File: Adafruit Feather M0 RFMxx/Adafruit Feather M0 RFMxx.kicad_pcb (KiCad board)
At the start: 2 copper layers, 50.8 x 22.9 mm, 39 parts, among them SW1 SPST_TACT-KMR2, U2 AP2112K-3.3, U3 MCP73831T-2ACI/OT, U4 RFM69HCW, X1 JSTPH, X2 32.768, X3 microUSB, X4 uFL

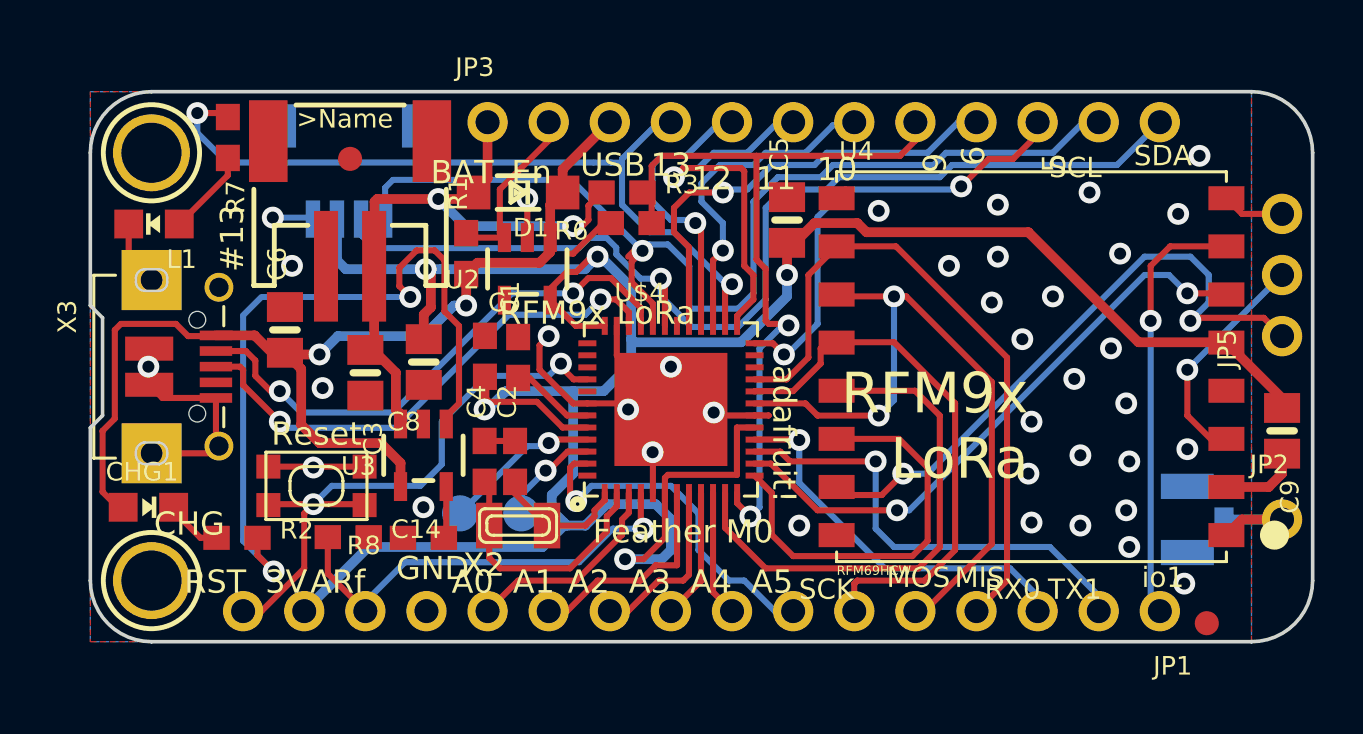
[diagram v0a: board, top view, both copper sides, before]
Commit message: Moving silscreen around and made some invisible. Working on a track near 144, 100.
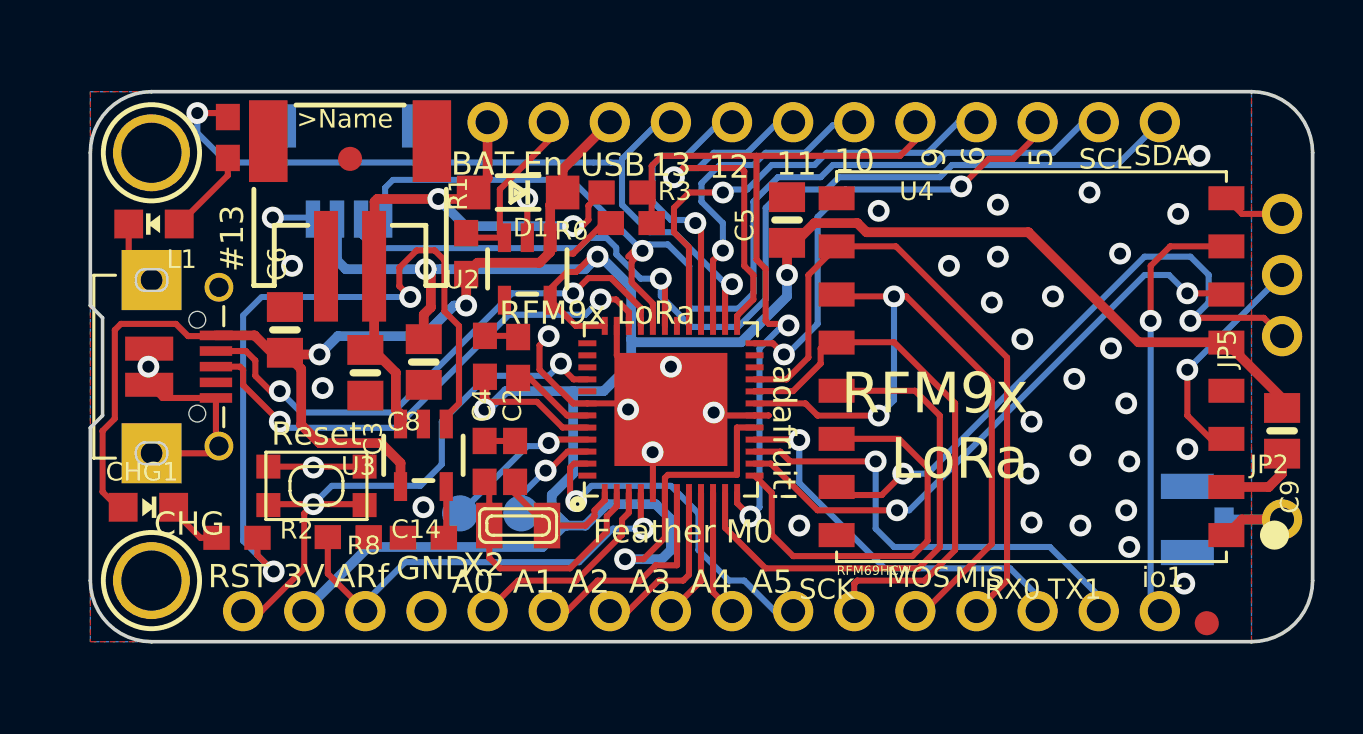
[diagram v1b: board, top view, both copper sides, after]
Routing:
- net GND: track 46.8 -> 47.9 mm

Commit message: Remaining Air wire was caused by ground pour on bottom that had become an island with the addition of the qwiic connector. Rerouted signals in that area to allow it to reconnect with other ground pour.
Now only "not connected" are defined ground area top and bottom.

Added gnd track between voltage sense resistor divider and ground so that it
shows when highlighting the GND net.

Moved track within USB connector to eliminate DRC "track too close to ..." error.

Now only 2 DRC errors are with holes in PCB that are part of X3 (USB connector).

Cleaned up silkscreen.

Plotted gerbers with option to not print silkscreen where there is no soldermask.
Option to not print silkscreen on pads did not seem to do anything.
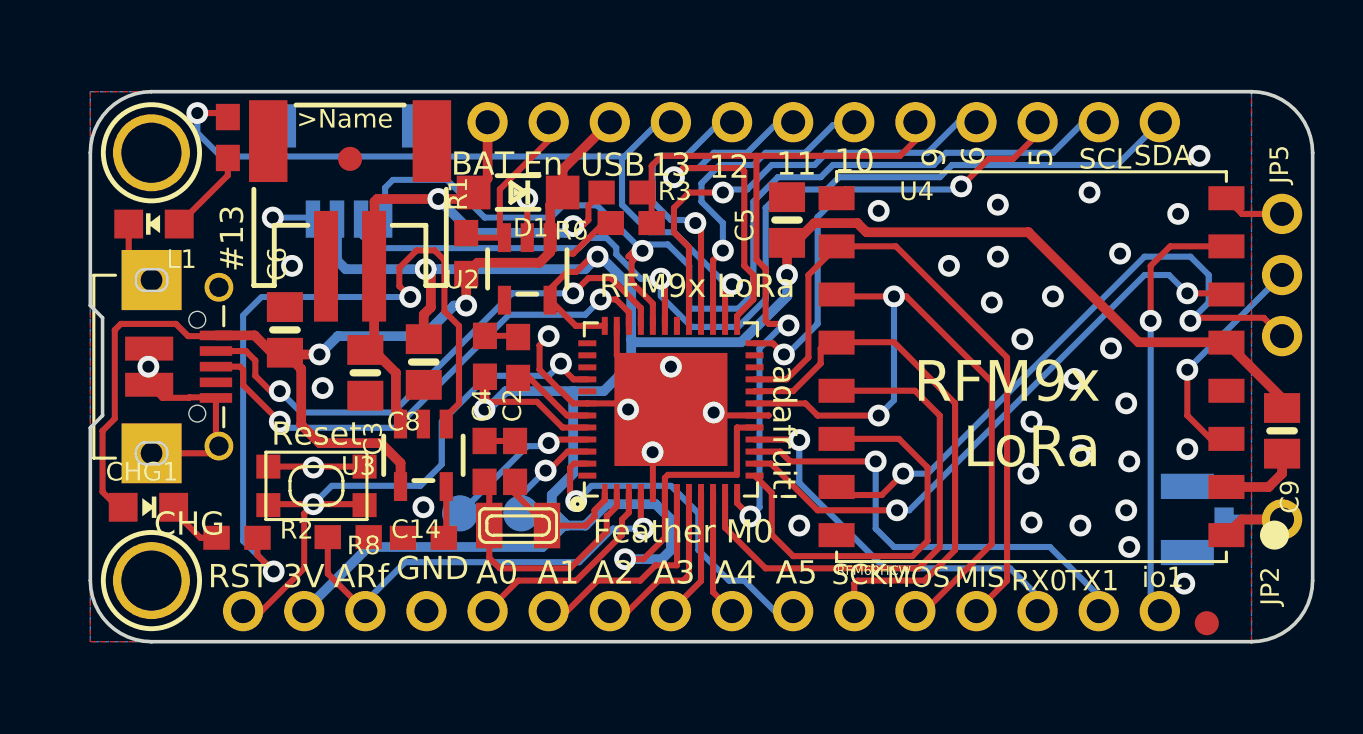
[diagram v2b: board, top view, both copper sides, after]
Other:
- board text added: "ATSAMD21G18 3.3V qwiic v0.1"
- board text removed: "ATSAMD21G18 3.3V"

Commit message: Added routing and vias to get SAMD21 pins 23 and 24 routed.
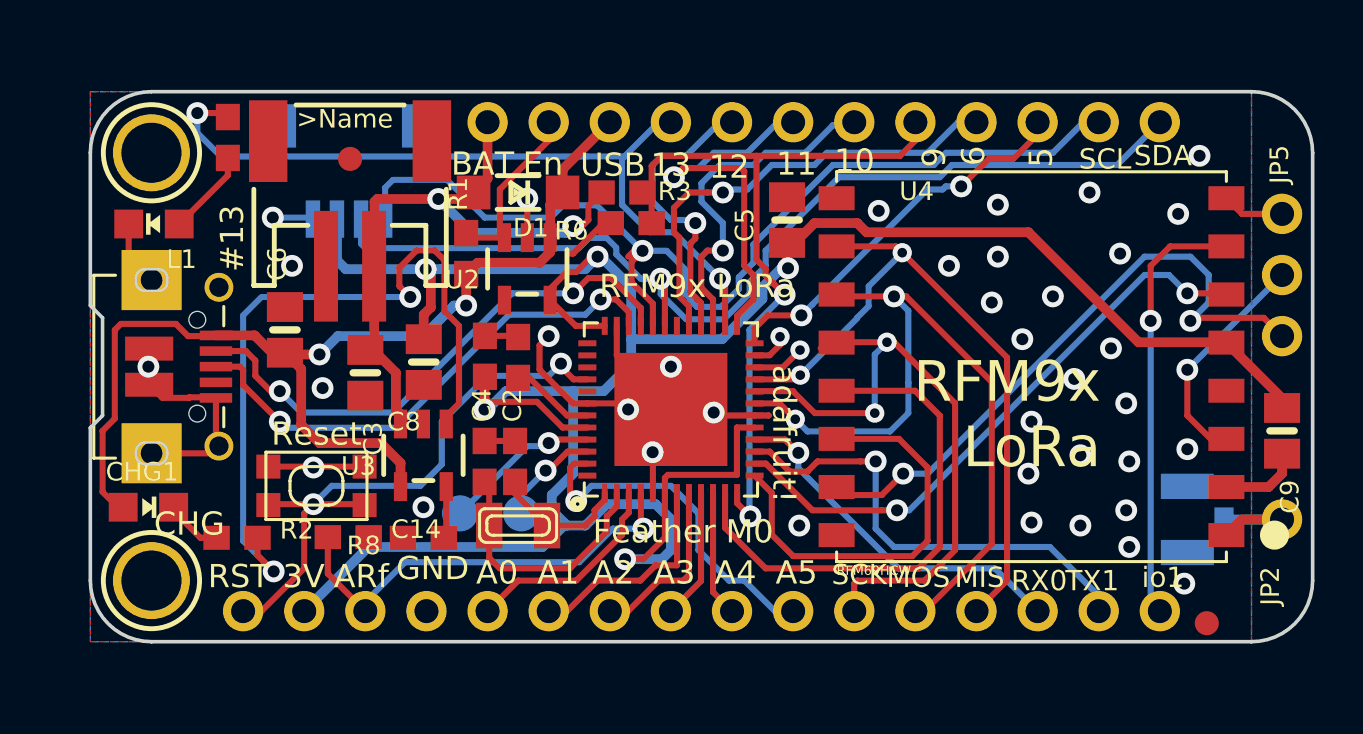
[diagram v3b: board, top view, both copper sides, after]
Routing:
- net /SCK: track 22.6 -> 27.3 mm, vias 0 -> 2
- net /D5: track 18.9 -> 16.2 mm
- net /SCL: track 44.8 -> 42.6 mm
- net Net-(U$4-Pad22): track 0.00 -> 2.19 mm, vias 0 -> 1
- net /MOSI: track 29.7 -> 31.6 mm
- net /SDA: track 44.2 -> 42.5 mm
- net /D2: track 0.00 -> 1.58 mm, vias 0 -> 1
- net /MISO: track 27.8 -> 28.9 mm, vias 0 -> 2
- net /D0: track 16.2 -> 15.1 mm
- net /D10: track 13.9 -> 14.6 mm
- net /D9: track 32.9 -> 32.2 mm

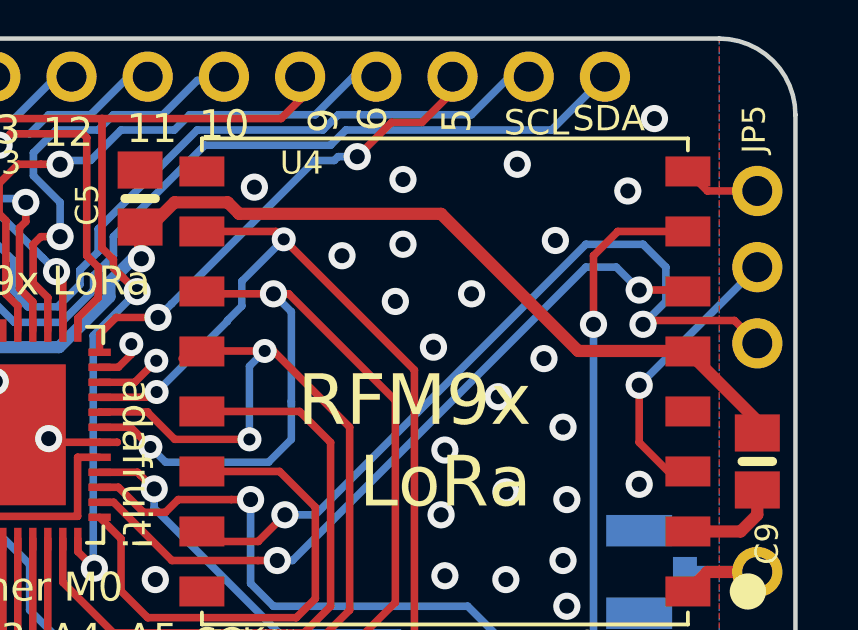
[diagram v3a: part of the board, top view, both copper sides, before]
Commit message: Added SPI flash from Adafruit Feather M0 Express. Still need to: - change 2 connections to RFM to other available pins - connect flash in schematic - route Note: the Netlist import complained about changing footprint for JP7 (qwiic connector)
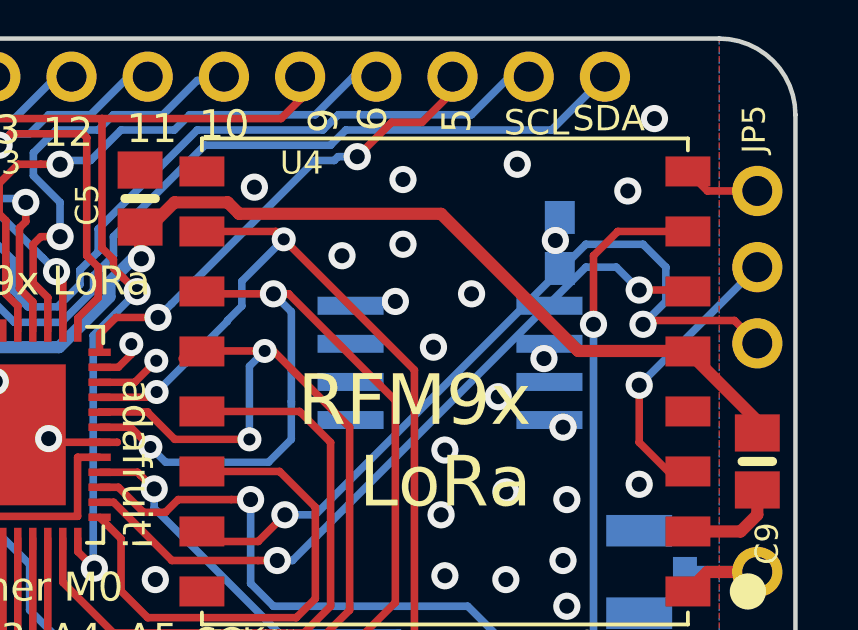
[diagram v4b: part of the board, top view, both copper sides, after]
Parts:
- added R4: 10K, Adafruit Feather M0 RFMxx:0603-NO, B.Cu at (166.0, 100.4)
- added U1: 2MB Flash, Adafruit Feather M0 RFMxx:SOIC8_208MIL, B.Cu at (162.4, 104.4)
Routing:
- net GND: vias 37 -> 35
- net /FLASH_CS: vias 0 -> 1
- net +3V3: vias 5 -> 6
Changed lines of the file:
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@@
     (tracks 703)
     (zones 0)
-    (modules 39)
-    (nets 58)
+    (modules 41)
+    (nets 62)
   )
   (page A4)
   (layers
-    (0 Top signal hide)
+    (0 Top signal)
     (31 Bottom signal)
     (32 B.Adhes user hide)
@@
   (net 56 "Net-(L1-PadA)")
   (net 57 "Net-(CHG1-PadC)")
+  (net 58 /FLASH_CS)
+  (net 59 /D2_FLASHMISO)
+  (net 60 /D3_FLASHSCK)
+  (net 61 /D4_FLASHMOSI)
   (net_class Default "This is the default net class."
     (clearance 0.2)
@@
     (add_net /D13)
     (add_net /D2)
+    (add_net /D2_FLASHMISO)
+    (add_net /D3_FLASHSCK)
     (add_net /D3_IRQ)
+    (add_net /D4_FLASHMOSI)
     (add_net /D4_RST)
     (add_net /D5)
@@
     (add_net /DIO5)
     (add_net /EN)
+    (add_net /FLASH_CS)
     (add_net /MISO)
     (add_net /MOSI)
@@
     (pad 6 smd rect (at 5.8 0.786) (size 1.2 1.8) (layers Bottom B.Paste B.Mask))
   )
+  (module "Adafruit Feather M0 RFMxx:0603-NO" (layer Bottom)
+    (at 166.047777 100.387611 90)
+    (fp_text reference R4 (at 1.778 -0.127 90) (layer B.SilkS)
+      (effects (font (size 0.77216 0.77216) (thickness 0.138988)) (justify left bottom mirror))
+    )
+    (fp_text value 10K (at 1.778 -0.762 90) (layer B.Fab)
+      (effects (font (size 0.77216 0.77216) (thickness 0.077216)) (justify left bottom mirror))
+    )
+    (fp_line (start -1.473 0.729) (end 1.473 0.729) (layer Dwgs.User) (width 0.0508))
+    (fp_line (start 1.473 0.729) (end 1.473 -0.729) (layer Dwgs.User) (width 0.0508))
+    (fp_line (start 1.473 -0.729) (end -1.473 -0.729) (layer Dwgs.User) (width 0.0508))
+    (fp_line (start -1.473 -0.729) (end -1.473 0.729) (layer Dwgs.User) (width 0.0508))
+    (fp_line (start -0.356 0.432) (end 0.356 0.432) (layer B.Fab) (width 0.1016))
+    (fp_line (start -0.356 -0.419) (end 0.356 -0.419) (layer B.Fab) (width 0.1016))
+    (fp_poly (pts (xy -0.8382 -0.4699) (xy -0.3381 -0.4699) (xy -0.3381 0.4801) (xy -0.8382 0.4801)) (layer B.Fab) (width 0))
+    (fp_poly (pts (xy 0.3302 -0.4699) (xy 0.8303 -0.4699) (xy 0.8303 0.4801) (xy 0.3302 0.4801)) (layer B.Fab) (width 0))
+    (fp_poly (pts (xy -0.1999 -0.3) (xy 0.1999 -0.3) (xy 0.1999 0.3) (xy -0.1999 0.3)) (layer B.Adhes) (width 0))
+    (pad 1 smd rect (at -0.85 0 90) (size 1.1 1) (layers Bottom B.Paste B.Mask)
+      (net 58 /FLASH_CS) (solder_mask_margin 0.0508))
+    (pad 2 smd rect (at 0.85 0 90) (size 1.1 1) (layers Bottom B.Paste B.Mask)
+      (net 2 +3V3) (solder_mask_margin 0.0508))
+  )
+  (module "Adafruit Feather M0 RFMxx:SOIC8_208MIL" (layer Bottom)
+    (at 162.387178 104.384411 90)
+    (descr "<b>Small Outline IC - 208mil Wide</b>")
+    (fp_text reference U1 (at -1.905 0.635 270) (layer B.SilkS)
+      (effects (font (size 0.77216 0.77216) (thickness 0.138988)) (justify right top mirror))
+    )
+    (fp_text value "2MB Flash" (at -1.905 -0.381 270) (layer B.Fab)
+      (effects (font (size 0.38608 0.38608) (thickness 0.038608)) (justify right top mirror))
+    )
+    (fp_line (start 2.4 2.615) (end 2.4 -2.615) (layer B.Fab) (width 0.2032))
+    (fp_line (start 2.4 -2.615) (end -2.4 -2.615) (layer B.Fab) (width 0.2032))
+    (fp_line (start -2.4 -2.615) (end -2.4 2.615) (layer B.Fab) (width 0.2032))
+    (fp_line (start -2.4 2.615) (end 2.4 2.615) (layer B.Fab) (width 0.2032))
+    (fp_line (start -2.4 -1.9) (end -2.4 1.9) (layer B.SilkS) (width 0.2032))
+    (fp_line (start 2.4 1.9) (end 2.4 -1.9) (layer B.SilkS) (width 0.2032))
+    (fp_circle (center -1.9304 -0.889) (end -1.6764 -0.889) (layer B.SilkS) (width 0.2032))
+    (fp_poly (pts (xy -2.15 -3.815) (xy -1.66 -3.815) (xy -1.66 -2.715) (xy -2.15 -2.715)) (layer B.Fab) (width 0))
+    (fp_poly (pts (xy -0.88 -3.815) (xy -0.39 -3.815) (xy -0.39 -2.715) (xy -0.88 -2.715)) (layer B.Fab) (width 0))
+    (fp_poly (pts (xy 0.39 -3.815) (xy 0.88 -3.815) (xy 0.88 -2.715) (xy 0.39 -2.715)) (layer B.Fab) (width 0))
+    (fp_poly (pts (xy 1.66 -3.815) (xy 2.15 -3.815) (xy 2.15 -2.715) (xy 1.66 -2.715)) (layer B.Fab) (width 0))
+    (fp_poly (pts (xy 1.66 2.715) (xy 2.15 2.715) (xy 2.15 3.815) (xy 1.66 3.815)) (layer B.Fab) (width 0))
+    (fp_poly (pts (xy 0.39 2.715) (xy 0.88 2.715) (xy 0.88 3.815) (xy 0.39 3.815)) (layer B.Fab) (width 0))
+    (fp_poly (pts (xy -0.88 2.715) (xy -0.39 2.715) (xy -0.39 3.815) (xy -0.88 3.815)) (layer B.Fab) (width 0))
+    (fp_poly (pts (xy -2.15 2.715) (xy -1.66 2.715) (xy -1.66 3.815) (xy -2.15 3.815)) (layer B.Fab) (width 0))
+    (pad 2 smd rect (at -0.635 -3.315 90) (size 0.6 2.2) (layers Bottom B.Paste B.Mask)
+      (net 59 /D2_FLASHMISO) (solder_mask_margin 0.0508))
+    (pad 7 smd rect (at -0.635 3.315 90) (size 0.6 2.2) (layers Bottom B.Paste B.Mask)
+      (net 2 +3V3) (solder_mask_margin 0.0508))
+    (pad 1 smd rect (at -1.905 -3.315 90) (size 0.6 2.2) (layers Bottom B.Paste B.Mask)
+      (net 58 /FLASH_CS) (solder_mask_margin 0.0508))
+    (pad 3 smd rect (at 0.635 -3.315 90) (size 0.6 2.2) (layers Bottom B.Paste B.Mask)
+      (net 2 +3V3) (solder_mask_margin 0.0508))
+    (pad 4 smd rect (at 1.905 -3.315 90) (size 0.6 2.2) (layers Bottom B.Paste B.Mask)
+      (net 1 GND) (solder_mask_margin 0.0508))
+    (pad 8 smd rect (at -1.905 3.315 90) (size 0.6 2.2) (layers Bottom B.Paste B.Mask)
+      (net 2 +3V3) (solder_mask_margin 0.0508))
+    (pad 6 smd rect (at 0.635 3.315 90) (size 0.6 2.2) (layers Bottom B.Paste B.Mask)
+      (net 60 /D3_FLASHSCK) (solder_mask_margin 0.0508))
+    (pad 5 smd rect (at 1.905 3.315 90) (size 0.6 2.2) (layers Bottom B.Paste B.Mask)
+      (net 61 /D4_FLASHMOSI) (solder_mask_margin 0.0508))
+  )
   (gr_poly (pts (xy 164.338 100.33) (xy 156.337 100.33) (xy 156.337 102.87) (xy 164.338 102.87)) (layer B.SilkS) (width 0.15))
   (gr_poly (pts (xy 165.481 108.585) (xy 156.21 108.585) (xy 156.21 110.617) (xy 165.481 110.617)) (layer B.SilkS) (width 0.15))
@@
   (via (at 160.5661 102.3366) (size 0.9064) (drill 0.5) (layers Top Bottom) (net 1))
   (via (at 164.2491 111.6076) (size 0.9064) (drill 0.5) (layers Top Bottom) (net 1))
-  (via (at 164.2491 108.6866) (size 0.9064) (drill 0.5) (layers Top Bottom) (net 1))
+  (via (at 164.2491 108.6866) (size 0.9064) (drill 0.5) (layers Top Bottom) (net 58))
   (via (at 162.0901 109.4486) (size 0.9064) (drill 0.5) (layers Top Bottom) (net 1))
-  (via (at 166.1541 106.5276) (size 0.9064) (drill 0.5) (layers Top Bottom) (net 1))
+  (via (at 166.1541 106.5276) (size 0.9064) (drill 0.5) (layers Top Bottom) (net 2))
   (via (at 166.1541 110.9726) (size 0.9064) (drill 0.5) (layers Top Bottom) (net 1))
   (via (at 163.9951 105.5116) (size 0.9064) (drill 0.5) (layers Top Bottom) (net 1))

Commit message: Maybe in last commit: - Added spi flash footprint from Adafruit Feather M0 Express. - changed footprint of imported resistor for SPI flash to same as other 0603's.
Removed extraneous small track on SDA on TOP.
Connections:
- U$4 pad 22: Net-(U$4-Pad22) -> /FLASH_CS
- U$4 pad 23: /D2 -> /D2_FLASHMISO
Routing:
- net Net-(U$4-Pad22): track 2.19 -> 0.00 mm, vias 1 -> 0
- net /FLASH_CS: track 0.00 -> 2.19 mm, vias 1 -> 2
- net /D2_FLASHMISO: track 0.00 -> 1.58 mm, vias 0 -> 1
- net /D2: track 1.58 -> 0.00 mm, vias 1 -> 0

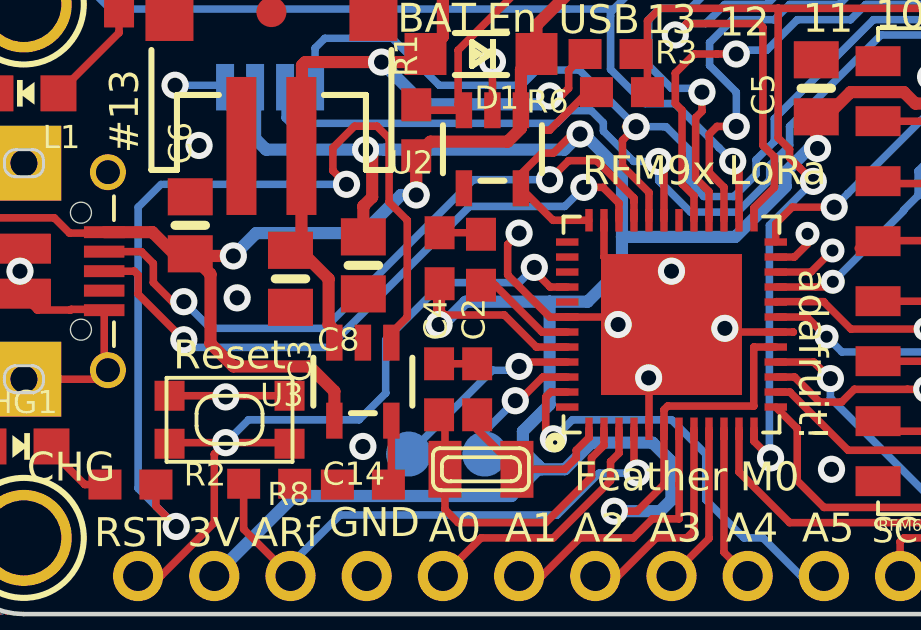
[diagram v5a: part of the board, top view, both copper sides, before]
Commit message: Before moving runners around for room for new traces.
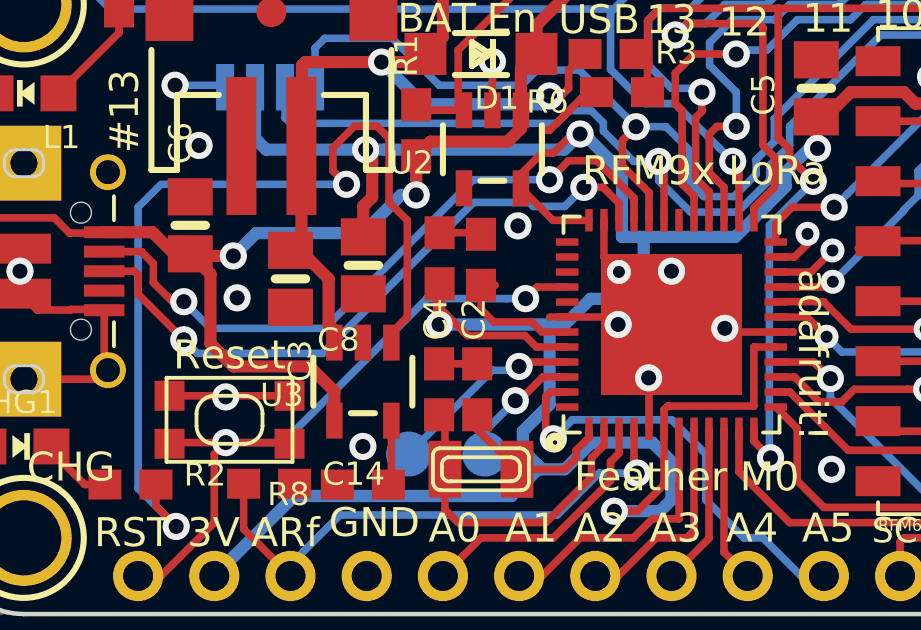
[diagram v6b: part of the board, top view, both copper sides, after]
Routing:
- net GND: track 47.9 -> 45.1 mm, vias 35 -> 36
- net /~RESET: track 25.5 -> 23.8 mm
- net Net-(C1-Pad1): track 3.52 -> 4.46 mm
